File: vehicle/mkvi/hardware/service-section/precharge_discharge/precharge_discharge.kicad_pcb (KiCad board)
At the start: 2 copper layers, 127 x 72.1 mm, 29 parts, among them J1 MicroFit_VT_5x1, J2 Automotive_M.2_Edge_Connector, K1 G2RG-2A-X_DC12, K2 3350-4275-126, Q1 SSM3K333R, U1 MCP6001, U2 MCP6001, U3 MCP6001

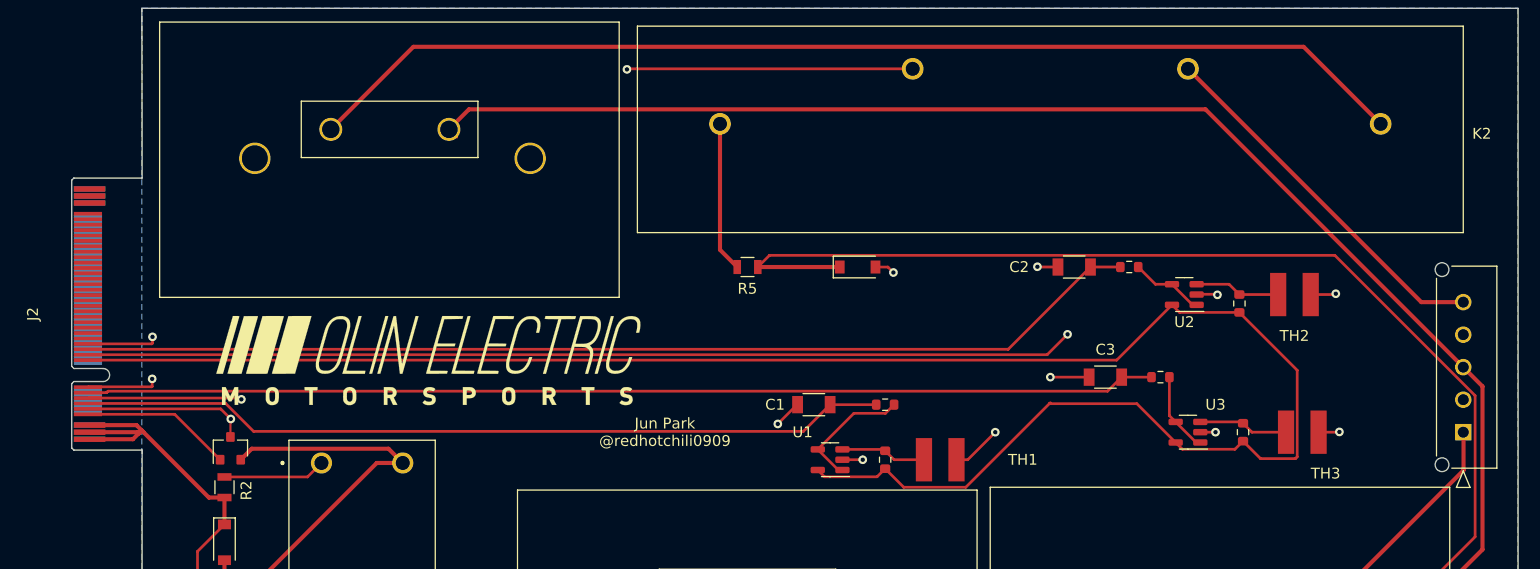
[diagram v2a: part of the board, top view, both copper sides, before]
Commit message: feat: updates from layout checklist
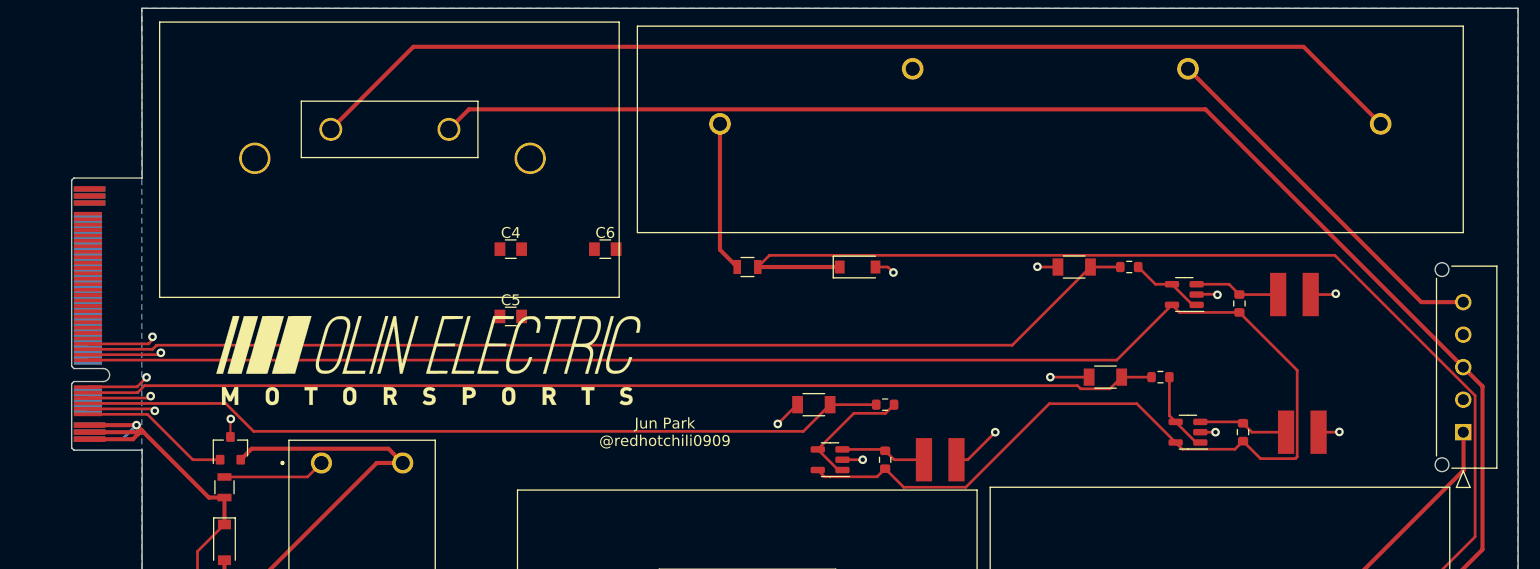
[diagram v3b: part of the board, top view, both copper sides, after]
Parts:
- added C4: C_0.1uF, footprints:C_0805_OEM, F.Cu at (100.1, 84.7)
- added C5: C_0.1uF, footprints:C_0805_OEM, F.Cu at (100.1, 90.9)
- added C6: C_0.1uF, footprints:C_0805_OEM, F.Cu at (108.8, 84.7)
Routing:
- net GND: track 184.3 -> 57.0 mm
- net /FINAL_SHUTDOWN: track 261.4 -> 275.1 mm, vias 0 -> 1
- net /HV_TS+: track 229.5 -> 228.4 mm

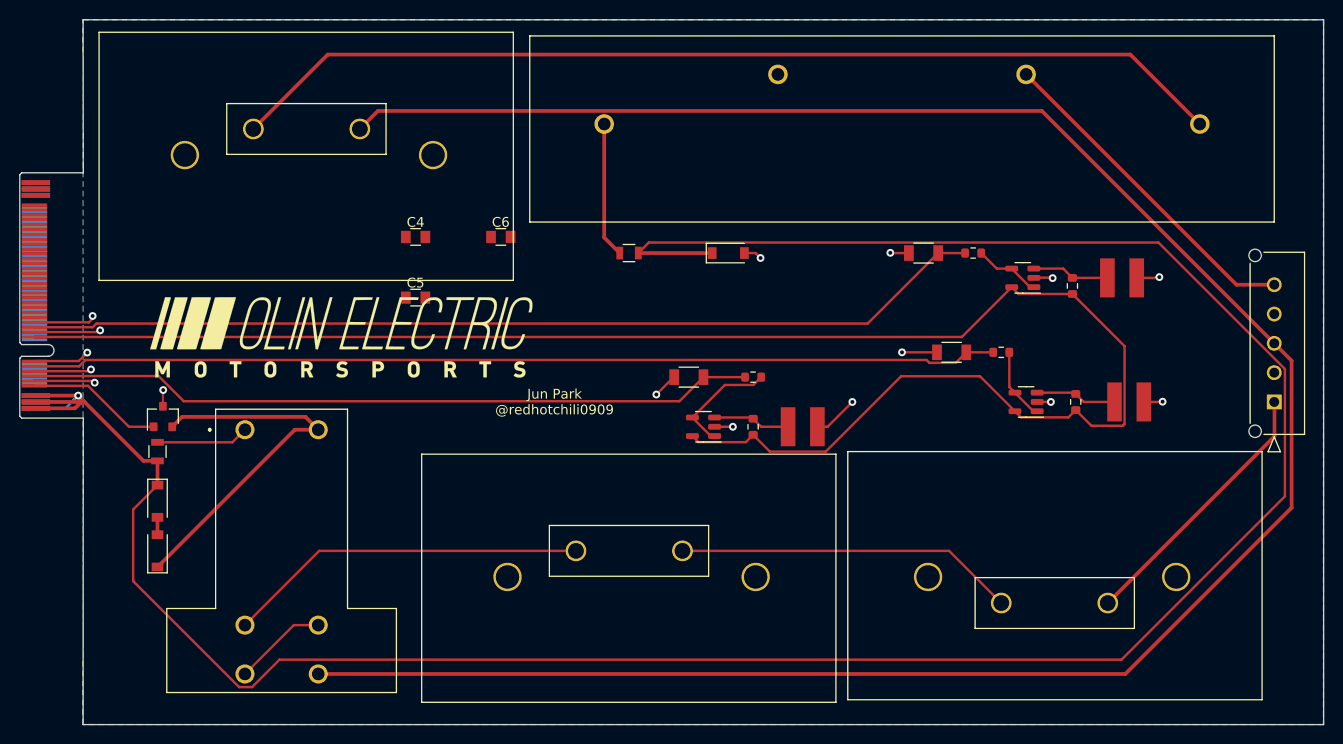
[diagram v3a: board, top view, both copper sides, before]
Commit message: V3. Precharge_Discharge PCB Layout
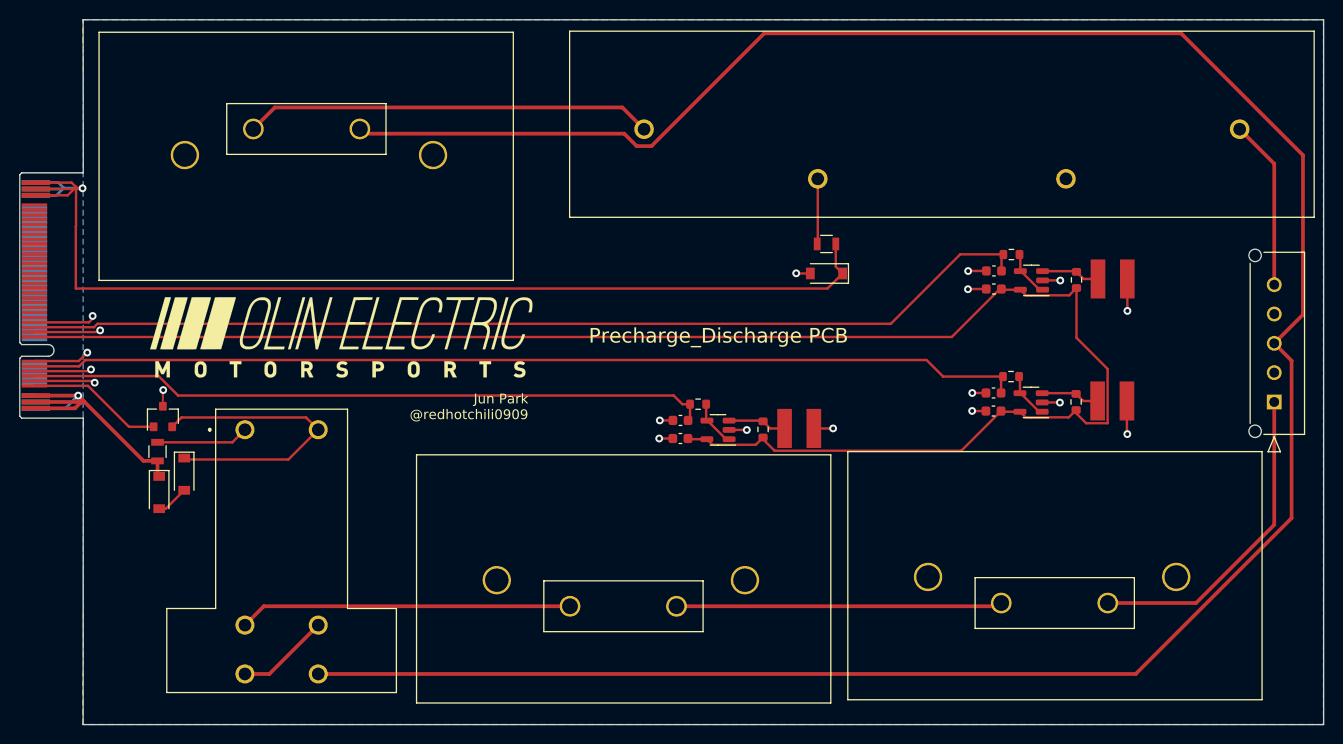
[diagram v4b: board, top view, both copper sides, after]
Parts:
- C1, C2, C3: footprint footprints:C_1206_OEM -> OEM:C_0603
- C4, C5, C6: footprint footprints:C_0805_OEM -> OEM:C_0603
- moved K2 74.1 mm to (188.2, 66.2), turned to 180 degrees
- moved C5 59.2 mm to (159.3, 90.0), turned to 180 degrees
- moved C6 53.5 mm to (159.2, 102.5), turned to 180 degrees
- moved C4 34.1 mm to (127.2, 105.3), turned to 180 degrees
- moved R5 20.2 mm to (142.1, 85.4)
- moved R3 12.8 mm to (115.9, 122.5), turned to 0 degrees
- moved D3 10.3 mm to (142.1, 88.5), turned to 180 degrees
- moved D2 8.31 mm to (76.4, 109.0), turned to -90 degrees
- moved C2 7.44 mm to (159.3, 88.2)
- moved R8 6.27 mm to (129.0, 101.8)
- moved C3 5.98 mm to (159.2, 100.7)
- moved C1 4.51 mm to (127.2, 103.5)
- moved R10 3.92 mm to (161.1, 86.5)
- moved R12 2.67 mm to (161.0, 99.0)
- moved TH3 1.73 mm to (171.4, 101.5)
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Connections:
- J2 pad P38: unconnected-(J2-PadP38) -> /FINAL_SHUTDOWN
- J2 pad P39: unconnected-(J2-PadP39) -> /FINAL_SHUTDOWN
- J2 pad P40: unconnected-(J2-PadP40) -> /FINAL_SHUTDOWN
- K2 pad 2: /HV_TS- -> Net-(K2-Pad2)
- K2 pad 4: Net-(K2-Pad4) -> /HV_TS-
- R3 pad 1: Net-(R3-Pad1) -> Net-(K1-Pad3)
- R3 pad 2: Net-(K1-Pad3) -> Net-(R3-Pad2)
- R4 pad 1: Net-(R3-Pad1) -> Net-(R3-Pad2)
- R5 pad 2: Net-(K2-Pad4) -> Net-(K2-Pad2)
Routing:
- net /FINAL_SHUTDOWN: track 275.1 -> 158.0 mm, vias 1 -> 2
- net Net-(K2-Pad1): track 103.0 -> 41.8 mm
- net Net-(R3-Pad1): track 34.8 -> 0.00 mm
- net Net-(R3-Pad2): track 0.00 -> 33.4 mm
- net /HV_TS+: track 228.4 -> 252.5 mm
- net /HV_TS-: track 34.3 -> 17.4 mm
- net Net-(K2-Pad4): track 13.9 -> 0.00 mm
- net /PRECHARGE_COIL: track 38.2 -> 30.9 mm
- net Net-(R8-Pad2): track 11.8 -> 4.77 mm
- net Net-(K2-Pad2): track 0.00 -> 6.69 mm
- net /TEMP_SENSE_DISCHARGE: track 98.4 -> 104.0 mm
- net /HV_BAT+: track 27.7 -> 32.9 mm
- net /TEMP_SENSE_PRECHARGE2: track 74.8 -> 70.0 mm
- net +5V: track 175.7 -> 172.0 mm
- net Net-(K1-Pad3): track 37.0 -> 34.1 mm
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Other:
- board text added: "12.10.22"
- board text added: "Precharge_Discharge PCB"
- board text added: "Rev. 1"

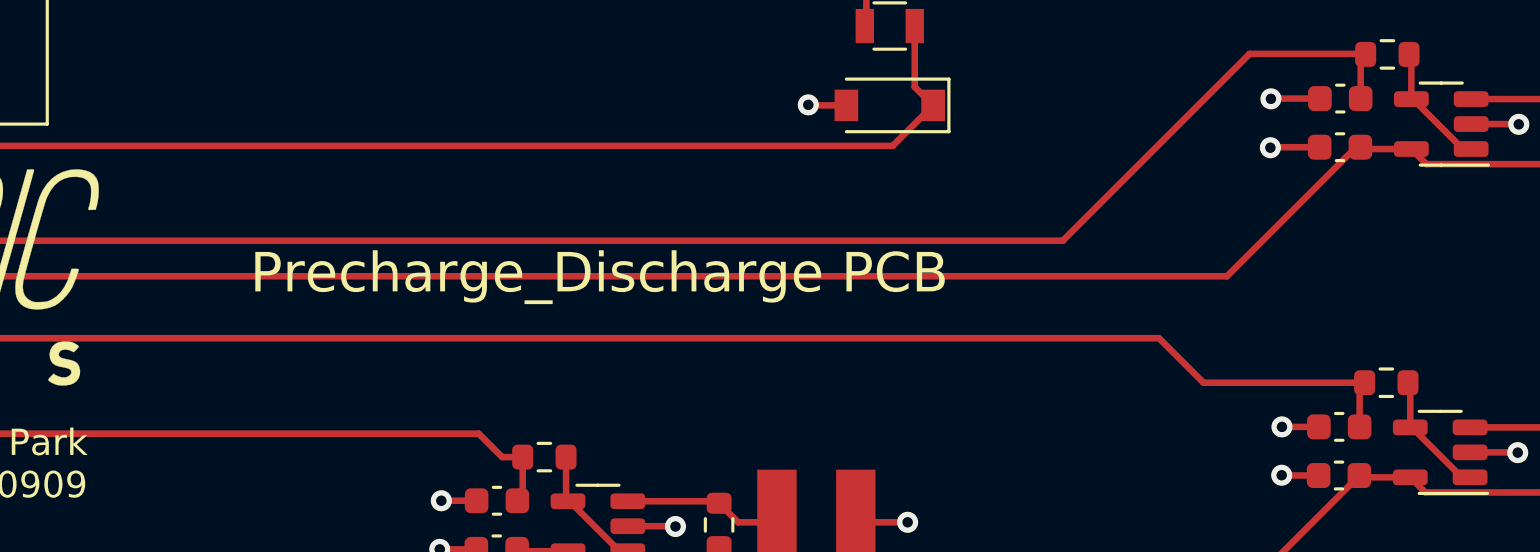
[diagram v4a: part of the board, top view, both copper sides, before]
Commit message: Added Silkscreen Design
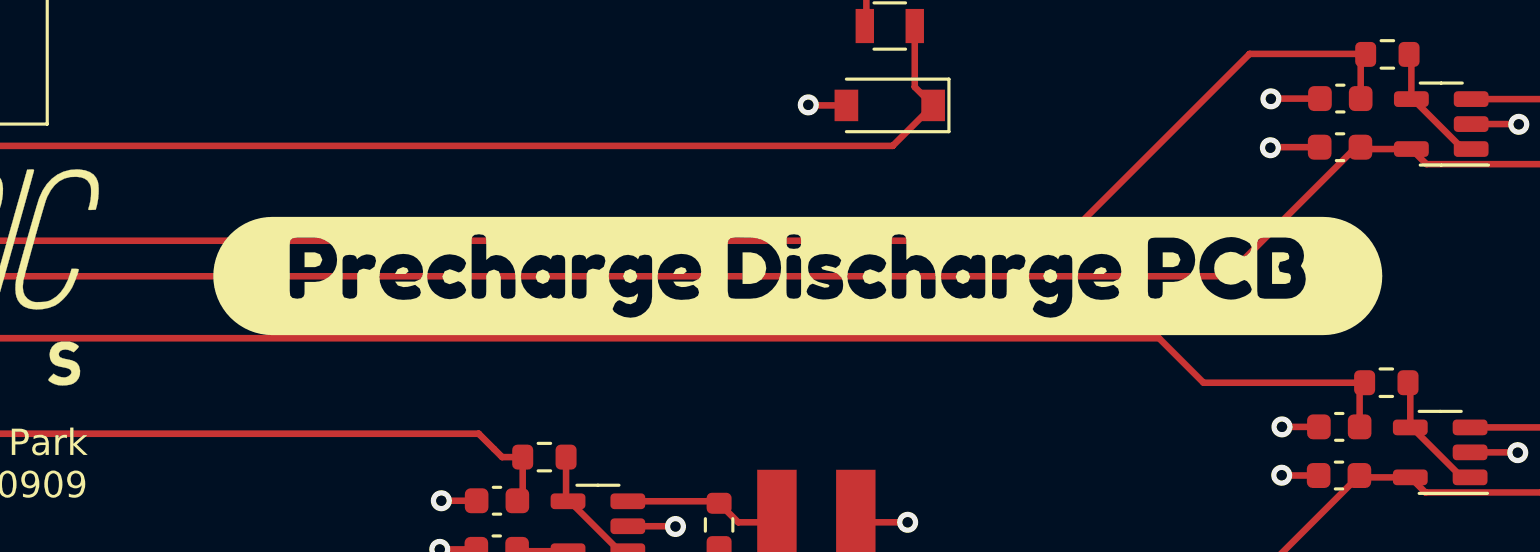
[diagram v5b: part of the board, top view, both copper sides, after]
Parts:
- added G1: LOGO, jun-library:star, B.Cu at (138.4, 106.2)
- added G2: LOGO, footprints:fromis, B.Cu at (72.7, 126.6)
- added G3: LOGO, footprints:kirbystar2, B.Cu at (108.9, 97.7)
- added kibuzzard-639639B8: G***, kibuzzard-639639B8, F.Cu at (138.6, 94.9)
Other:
- board text removed: "Precharge_Discharge PCB"

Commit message: Implmeneted Requested Changes
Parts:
- added R1: R_10K, footprints:R_0805_OEM, F.Cu at (71.2, 103.2)
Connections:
- Q1 pad 2: /PRECHARGE_COIL -> GND
- Q1 pad 3: GND -> /PRECHARGE_COIL
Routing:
- net GND: track 57.8 -> 59.6 mm, vias 19 -> 20
- net /PRECHARGE_COIL: track 30.9 -> 31.9 mm
- net /FINAL_SHUTDOWN: track 158.0 -> 157.3 mm
- net /HV_BAT+: track 32.9 -> 32.3 mm
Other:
- board text added: "MKVI_Rev. 1"
- board text removed: "Rev. 1"

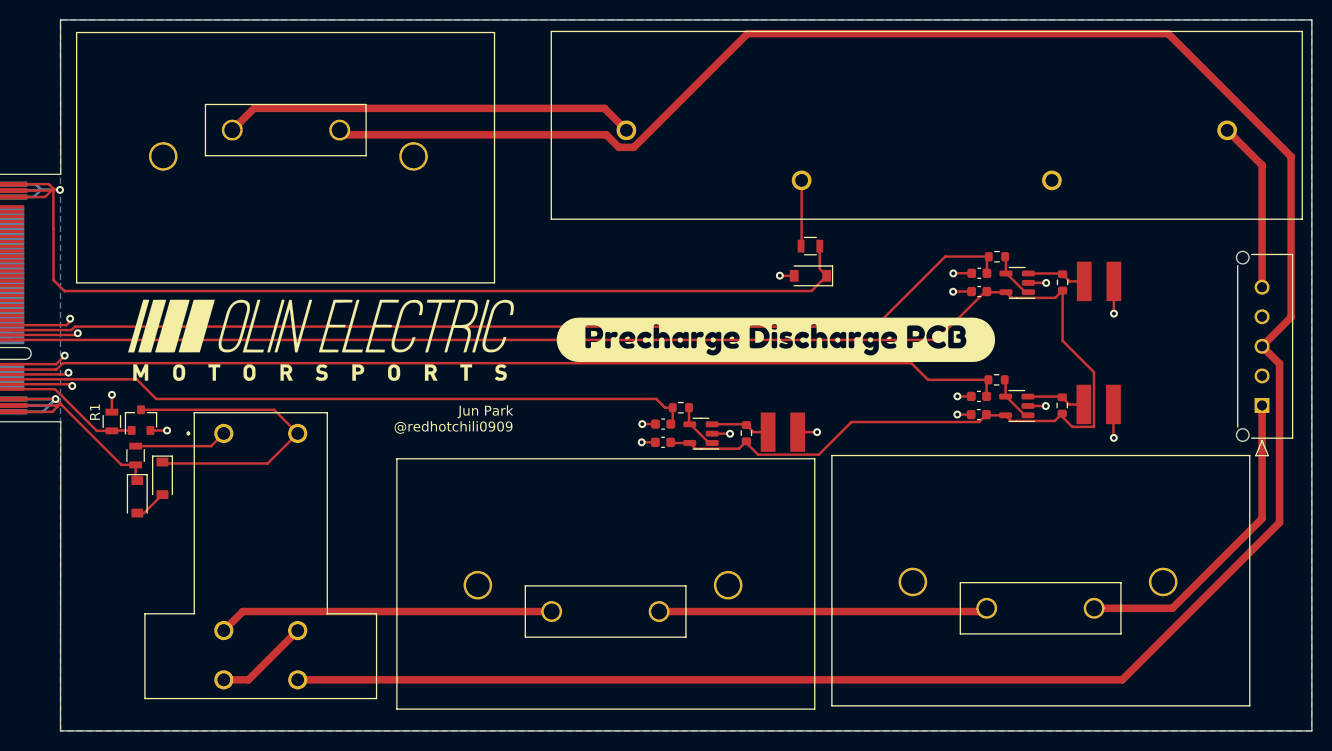
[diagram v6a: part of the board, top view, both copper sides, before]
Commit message: Revised PCB for correct  silkscreen measurements and ground layer
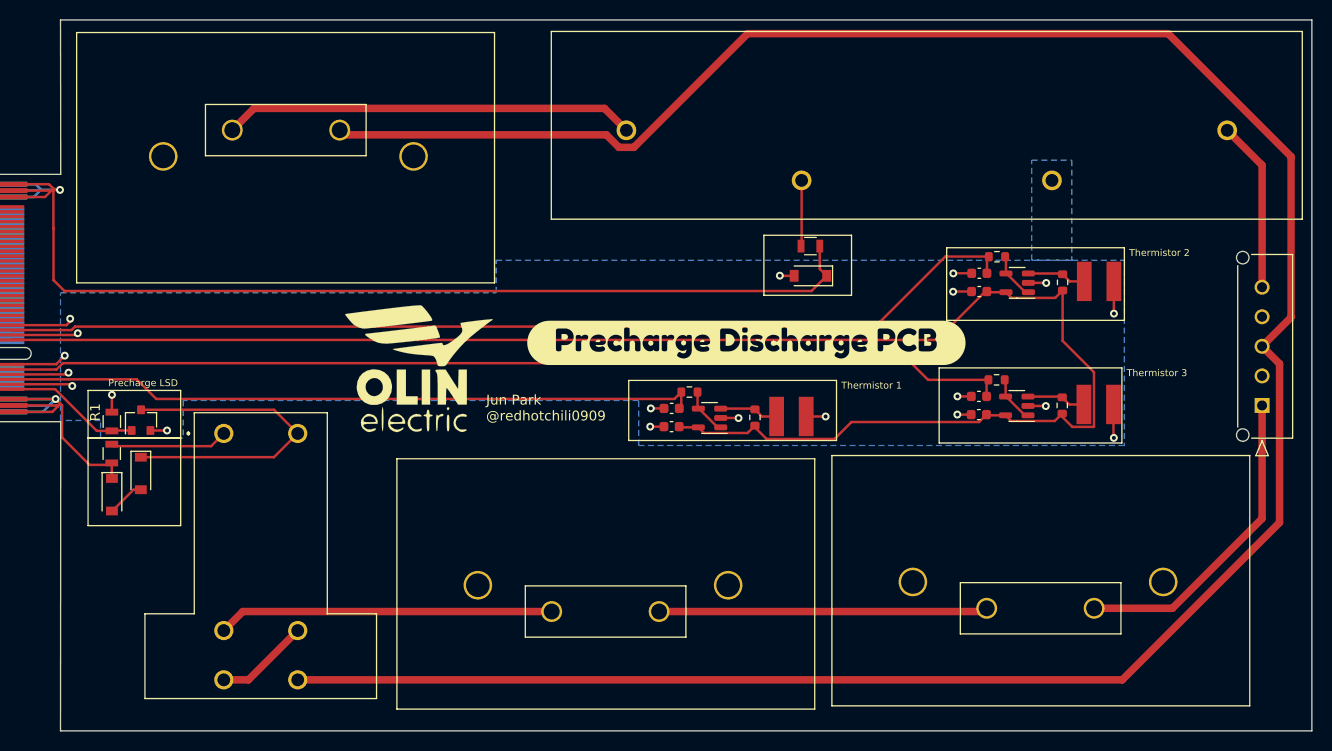
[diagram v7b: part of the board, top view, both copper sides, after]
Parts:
- removed the G*** at (92.5, 95.0)
- added G***: LOGO, footprints:Small_OE_Logo, F.Cu at (102.4, 97.8)
- moved kibuzzard-639639B8 3.01 mm to (135.6, 95.2)
- moved D1 2.58 mm to (71.3, 110.7)
- moved R2 2.43 mm to (71.2, 106.5)
- moved D2 2.25 mm to (74.2, 108.5)
- moved R7 1.81 mm to (136.5, 102.8)
- moved C4 1.81 mm to (128.0, 103.8)
- moved C1 1.81 mm to (128.1, 101.9)
- moved U1 1.81 mm to (131.9, 102.9)
- moved R8 1.81 mm to (129.9, 100.2)
- moved TH1 1.81 mm to (140.2, 102.7)
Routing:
- net Net-(K1-Pad1): track 9.48 -> 12.0 mm
- net /PRECHARGE_COIL: track 31.9 -> 33.8 mm
- net +5V: track 172.0 -> 170.5 mm
- net /TEMP_SENSE_PRECHARGE2: track 70.0 -> 70.8 mm
- net /FINAL_SHUTDOWN: track 157.3 -> 156.8 mm
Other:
- board text added: "Precharge LSD"
- board text added: "Thermistor 1"
- board text added: "Thermistor 2"
- board text added: "Thermistor 3"
